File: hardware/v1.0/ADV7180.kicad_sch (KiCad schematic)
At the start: 49 parts, among them J2 Conn_01x03, J3 Conn_01x04, J4 Conn_01x03, J5 Conn_01x34, U2 AMS1117-1.8, U3 ADV7180BCP32Z-RL, U4 TLV62585, Y1 28.63636MHz

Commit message: backup
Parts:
- removed D2: LED, LED_SMD:LED_0805_2012Metric, symbol Device:LED
- removed R7, R8: 270, Resistor_SMD:R_0603_1608Metric, symbol Device:R_Small
- J5: renamed from J2; footprint (none) -> Connector_PinHeader_2.54mm:PinHeader_1x03_P2.54mm_Vertical
- J6: renamed from J4; footprint (none) -> Connector_PinHeader_2.54mm:PinHeader_1x03_P2.54mm_Vertical
- renumbered C20 to C10, C12 to C11, C13 to C12, C16 to C13, C17 to C14, C14 to C15, C18 to C16, C21 to C17, C10 to C18, C11 to C19, C5 to C2, C22 to C20, C15 to C21, C19 to C22, C6 to C3, C2 to C4, C3 to C5, C4 to C6, C8 to C7, C7 to C8, J3 to J7, J5 to J8, R2 to R10, R3 to R11, R4 to R12, R6 to R13, R9 to R14, R10 to R15, R11 to R16, R5 to R8, R1 to R9, U2 to U3, U3 to U4, U4 to U5
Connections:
- net YUV_CLK: now also RN1.5 (R4.2), U4.11 (LLC); no longer J8.2 (Pin_2), RN4.1 (R1.1)
- net YUV_HS: now also RN1.6 (R3.2), U4.1 (HS); no longer J8.3 (Pin_3), RN3.4 (R4.1)
- net YUV_INTRQ: now also RN1.7 (R2.2), U4.32 (~{INTRQ}); no longer J8.4 (Pin_4), RN3.1 (R1.1)
- net YUV_P0: now also RN3.5 (R4.2), U4.16 (P0); no longer J8.22 (Pin_22), RN1.4 (R4.1)
- net YUV_P1: now also RN3.6 (R3.2), U4.15 (P1); no longer J8.23 (Pin_23), RN1.3 (R3.1)
- net YUV_P2: now also RN3.7 (R2.2), U4.10 (P2); no longer J8.24 (Pin_24), RN1.2 (R2.1)
- net YUV_P3: now also RN3.8 (R1.2), U4.9 (P3); no longer J8.25 (Pin_25), RN1.1 (R1.1)
- net YUV_P4: now also RN4.5 (R4.2), U4.8 (P4); no longer J8.26 (Pin_26), RN2.4 (R4.1)
- net YUV_P5: now also RN4.6 (R3.2), U4.7 (P5); no longer J8.27 (Pin_27), RN2.3 (R3.1)
- net YUV_P6: now also RN4.7 (R2.2), U4.6 (P6); no longer J8.28 (Pin_28), RN2.2 (R2.1)
- net YUV_P7: now also RN4.8 (R1.2), U4.5 (P7); no longer J8.29 (Pin_29), RN2.1 (R1.1)
- net YUV_SFL: now also RN2.5 (R4.2), U4.4 (SFL); no longer J8.6 (Pin_6), RN3.2 (R2.1)
- net YUV_VS: now also RN1.8 (R1.2), U4.31 (VS/FIELD); no longer J8.5 (Pin_5), RN3.3 (R3.1)
- net at RN2.6 (R3.2): no longer U4.7 (P5)
- net at RN2.7 (R2.2): no longer U4.6 (P6)
- net at RN2.8 (R1.2): no longer U4.5 (P7)
- net at RN4.2 (R2.1): now also J8.28 (Pin_28)
- net at RN4.3 (R3.1): now also J8.27 (Pin_27)
- net at RN4.4 (R4.1): now also J8.26 (Pin_26)
- new net: J8.29 (Pin_29), RN4.1 (R1.1)
- new net: J8.5 (Pin_5), RN1.1 (R1.1)
- new net: J8.4 (Pin_4), RN1.2 (R2.1)
- new net: J8.3 (Pin_3), RN1.3 (R3.1)
- new net: J8.2 (Pin_2), RN1.4 (R4.1)
- new net: J8.22 (Pin_22), RN3.4 (R4.1)
- new net: J8.23 (Pin_23), RN3.3 (R3.1)
- new net: J8.24 (Pin_24), RN3.2 (R2.1)
- new net: J8.25 (Pin_25), RN3.1 (R1.1)
- new net: J8.6 (Pin_6), RN2.4 (R4.1)
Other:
- moved on the sheet: J7, J8

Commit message: changes
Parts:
- added C40: 0.1uf, Capacitor_SMD:C_0603_1608Metric, symbol Device:C_Small
- added R36, R37: 4.7K, Resistor_SMD:R_0603_1608Metric, symbol Device:R_Small
- added TP1: VCC_PAD, TestPoint:TestPoint_Pad_D1.5mm, symbol Connector:TestPoint_Flag
- added TP2: SWIO_PAD, TestPoint:TestPoint_Pad_D1.5mm, symbol Connector:TestPoint_Flag
- added TP3: GND_PAD, TestPoint:TestPoint_Pad_D1.5mm, symbol Connector:TestPoint_Flag
- added U2: CH32V003JxMx, Package_SO:SOP-8_3.9x4.9mm_P1.27mm, symbol MCU_WCH_CH32V0:CH32V003JxMx
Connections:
- net +3V3: now also C40.1, R36.1, R37.1, TP1.1, U2.4 (VDD)
- net GND: now also C40.2, TP3.1, U2.2 (VSS)
- net RST: now also U2.7 (PC4)
- net SCLK: now also R37.2, U2.6 (PC2)
- net SDATA: now also R36.2, U2.5 (PC1)
- new net SWIO: TP2.1, U2.8 (PD1/PD4/PD5)
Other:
- note added: "FPC"
- note added: "MCU"
- note removed: "CONNECTORS"
- moved on the sheet: J7

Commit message: changes
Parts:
- removed C21: 0.1uf, Capacitor_SMD:C_0603_1608Metric, symbol Device:C_Small
- removed C22: 10nf, Capacitor_SMD:C_0603_1608Metric, symbol Device:C_Small
- R15, R16: footprint Resistor_SMD:R_0402_1005Metric -> Resistor_SMD:R_0603_1608Metric
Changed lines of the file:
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@@
 	(rectangle
 		(start 59.69 144.78)
-		(end 116.84 172.72)
+		(end 111.76 172.72)
 		(stroke
 			(width 0.508)
@@
 	)
 	(junction
-		(at 95.25 162.56)
-		(diameter 0)
-		(color 0 0 0 0)
-	)
-	(junction
 		(at 152.4 114.3)
 		(diameter 0)
@@
 	)
 	(junction
-		(at 104.14 167.64)
-		(diameter 0)
-		(color 0 0 0 0)
-	)
-	(junction
 		(at 107.315 125.095)
 		(diameter 0)
@@
 	)
 	(junction
-		(at 104.14 162.56)
-		(diameter 0)
-		(color 0 0 0 0)
-	)
-	(junction
 		(at 41.91 73.66)
 		(diameter 0)
@@
 	)
 	(junction
-		(at 95.25 167.64)
-		(diameter 0)
-		(color 0 0 0 0)
-	)
-	(junction
 		(at 73.66 78.74)
 		(diameter 0)
@@
 	(wire
 		(pts
-			(xy 95.25 167.64) (xy 104.14 167.64)
-		)
-		(stroke
-			(width 0)
-			(type default)
-		)
-	)
-	(wire
-		(pts
 			(xy 78.74 78.74) (xy 76.2 78.74)
 		)
@@
 		)
 	)
-	(wire
-		(pts
-			(xy 104.14 162.56) (xy 113.03 162.56)
-		)
-		(stroke
-			(width 0)
-			(type default)
-		)
-	)
 	(bus
 		(pts
@@
 	(wire
 		(pts
-			(xy 95.25 162.56) (xy 104.14 162.56)
-		)
-		(stroke
-			(width 0)
-			(type default)
-		)
-	)
-	(wire
-		(pts
 			(xy 52.07 102.87) (xy 52.07 104.14)
 		)
@@
 	(wire
 		(pts
-			(xy 104.14 167.64) (xy 113.03 167.64)
-		)
-		(stroke
-			(width 0)
-			(type default)
-		)
-	)
-	(wire
-		(pts
 			(xy 153.67 88.9) (xy 156.21 88.9)
 		)
@@
 			)
 		)
-		(property "Footprint" "Resistor_SMD:R_0402_1005Metric"
+		(property "Footprint" "Resistor_SMD:R_0603_1608Metric"
 			(at 107.315 127.635 0)
 			(effects
@@
 			)
 		)
-		(property "Footprint" "Resistor_SMD:R_0402_1005Metric"
+		(property "Footprint" "Resistor_SMD:R_0603_1608Metric"
 			(at 107.315 133.985 0)
 			(effects
@@
 	)
 	(symbol
-		(lib_id "Device:C_Small")
-		(at 113.03 165.1 0)
-		(unit 1)
-		(exclude_from_sim no)
-		(in_bom yes)
-		(on_board yes)
-		(dnp no)
-		(property "Reference" "C22"
-			(at 111.125 166.37 0)
-			(effects
-				(font
-					(size 1.27 1.27)
-				)
-				(justify right)
-			)
-		)
-		(property "Value" "10nf"
-			(at 111.125 164.465 0)
-			(effects
-				(font
-					(size 1.27 1.27)
-				)
-				(justify right)
-			)
-		)
-		(property "Footprint" "Capacitor_SMD:C_0603_1608Metric"
-			(at 113.03 165.1 0)
-			(effects
-				(font
-					(size 1.27 1.27)
-				)
-				(hide yes)
-			)
-		)
-		(property "Datasheet" "~"
-			(at 113.03 165.1 0)
-			(effects
-				(font
-					(size 1.27 1.27)
-				)
-				(hide yes)
-			)
-		)
-		(property "Description" ""
-			(at 113.03 165.1 0)
-			(effects
-				(font
-					(size 1.27 1.27)
-				)
-				(hide yes)
-			)
-		)
-		(pin "1"
-		)
-		(pin "2"
-		)
-		(instances
-			(project "QMTECH_XC7A100T-Expantion-Board"
-				(path "/1a66a179-6cc4-4048-836e-3eb434e9da88/856c4711-f246-4385-ad64-862f60e59bf4"
-					(reference "C22")
-					(unit 1)
-				)
-			)
-		)
-	)
-	(symbol
 		(lib_id "power:GND")
 		(at 68.58 154.94 0)
@@
 					(unit 1)
 				)
-			)
-		)
-	)
-	(symbol
-		(lib_id "Device:C_Small")
-		(at 104.14 165.1 0)
-		(unit 1)
-		(exclude_from_sim no)
-		(in_bom yes)
-		(on_board yes)
-		(dnp no)
-		(property "Reference" "C21"
-			(at 102.235 166.37 0)
-			(effects
-				(font
-					(size 1.27 1.27)
-				)
-				(justify right)
-			)
-		)
-		(property "Value" "0.1uf"
-			(at 102.235 164.465 0)
-			(effects
-				(font
-					(size 1.27 1.27)
-				)
-				(justify right)
-			)
-		)
-		(property "Footprint" "Capacitor_SMD:C_0603_1608Metric"
-			(at 104.14 165.1 0)
-			(effects
-				(font
-					(size 1.27 1.27)
-				)
-				(hide yes)
-			)
-		)
-		(property "Datasheet" "~"
-			(at 104.14 165.1 0)
-			(effects
-				(font
-					(size 1.27 1.27)
-				)
-				(hide yes)
-			)
-		)
-		(property "Description" ""
-			(at 104.14 165.1 0)
-			(effects
-				(font
-					(size 1.27 1.27)
-				)
-				(hide yes)
-			)
-		)
-		(pin "1"
-		)
-		(pin "2"
-		)
-		(instances
-			(project "QMTECH_XC7A100T-Expantion-Board"
-				(path "/1a66a179-6cc4-4048-836e-3eb434e9da88/856c4711-f246-4385-ad64-862f60e59bf4"
-					(reference "C21")
-					(unit 1)
-				)

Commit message: backup
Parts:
- removed C1, C9: 10uf, Capacitor_SMD:C_0805_2012Metric, symbol Device:C_Small
- removed C17: 22uf, Capacitor_SMD:C_0805_2012Metric, symbol Device:C_Small
- removed D1: LED, LED_SMD:LED_0805_2012Metric, symbol Device:LED
- removed U3: AMS1117-1.8, Package_TO_SOT_SMD:SOT-223-3_TabPin2, symbol Regulator_Linear:AMS1117-1.8
- added D1: ~, C779813:LED-SMD_4P-L1.6-W1.5-BR_TZ-P4-1615, symbol Device:LED_ARGB
- added U13: TLV75718PDRV, Package_SON:WSON-6-1EP_2x2mm_P0.65mm_EP1x1.6mm, symbol Regulator_Linear:TLV75718PDRV
- C10: value 22uf -> 4.7uf
- C20: value 22uf -> 10uf
- C4, C8: value 0.1uf -> 1uf
- L1: value 1uh -> 2.2uh
- R15: value 450K -> 450k
- R16: value 100K -> 100k
- R36, R37: value 4.7K -> 4.7k
- R8: value 10K -> 10k
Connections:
- net +1V8: now also U13.1 (OUT)
- net +3V3: now also U13.4 (EN), U13.6 (IN)
- net GND: now also D1.2 (RK), U13.3 (GND), U13.7 (GND)
- net at R13.1: now also D1.1 (A)
- net STATUS: now reaches U2.3 (PA2)
- net STATUS: now also D1.3 (GK)
- no-connect marks 23 -> 24
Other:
- moved on the sheet: C10, C20, L1, R13, R15, R16, U5

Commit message: changes
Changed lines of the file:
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@@
 		(stroke
 			(width 0)
-			(type dash)
+			(type solid)
 		)
 		(fill
@@
 		(stroke
 			(width 0)
-			(type dash)
+			(type solid)
 		)
 		(fill
@@
 		(stroke
 			(width 0)
-			(type dash)
+			(type solid)
 		)
 		(fill

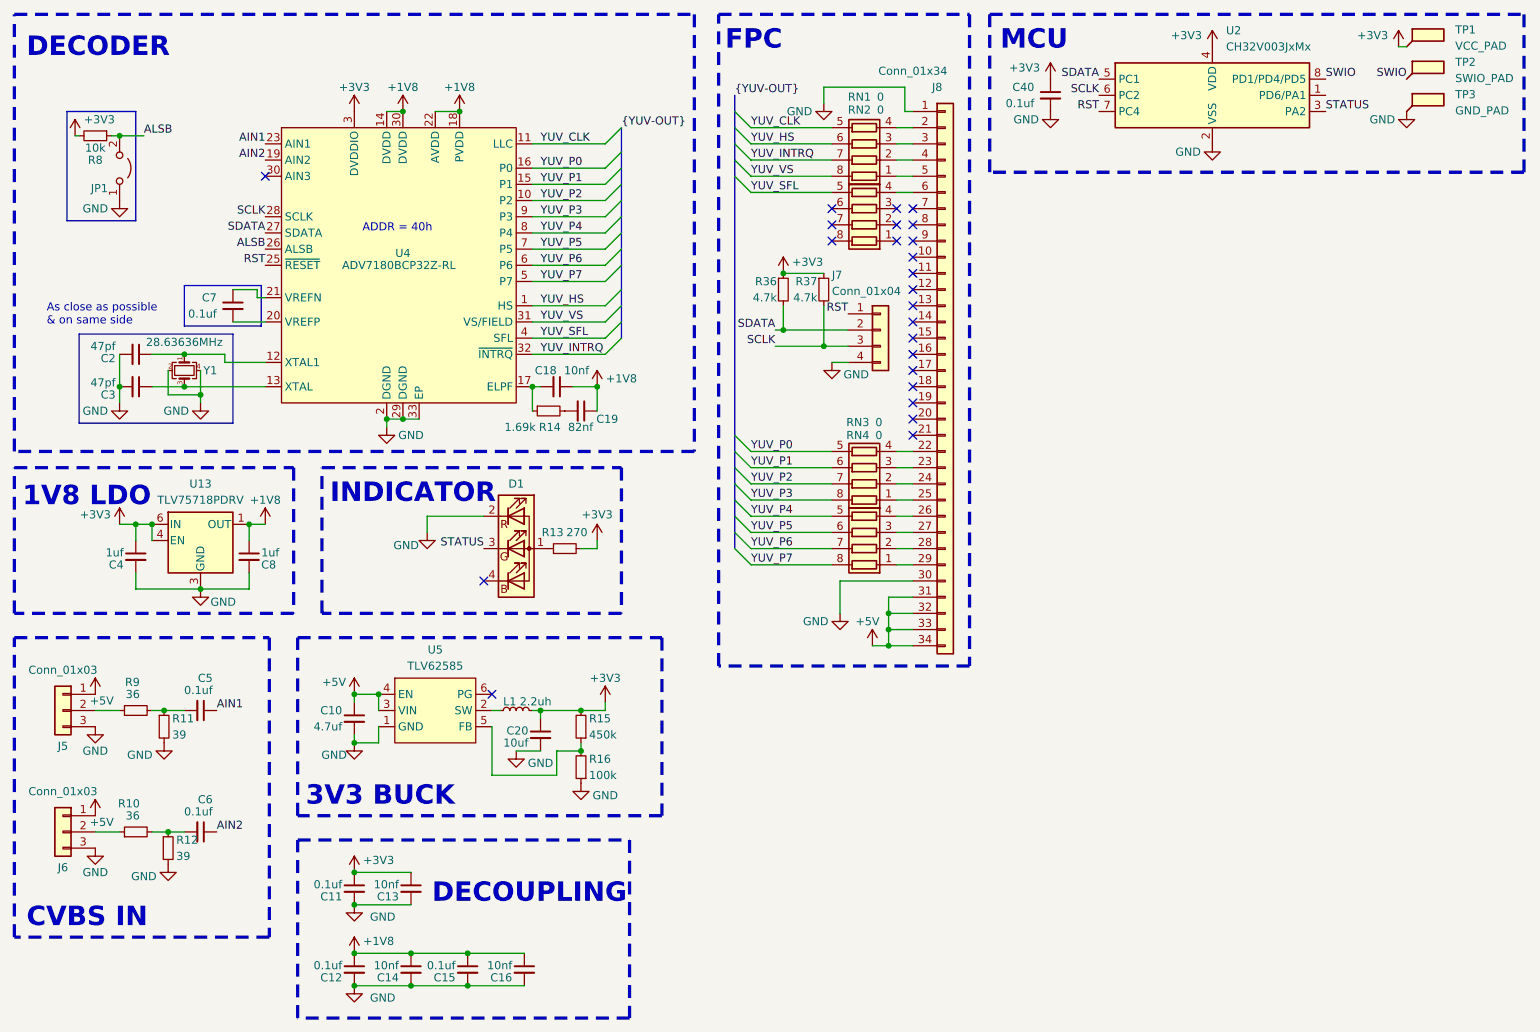
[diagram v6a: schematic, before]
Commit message: added pmod connectors instead of leds
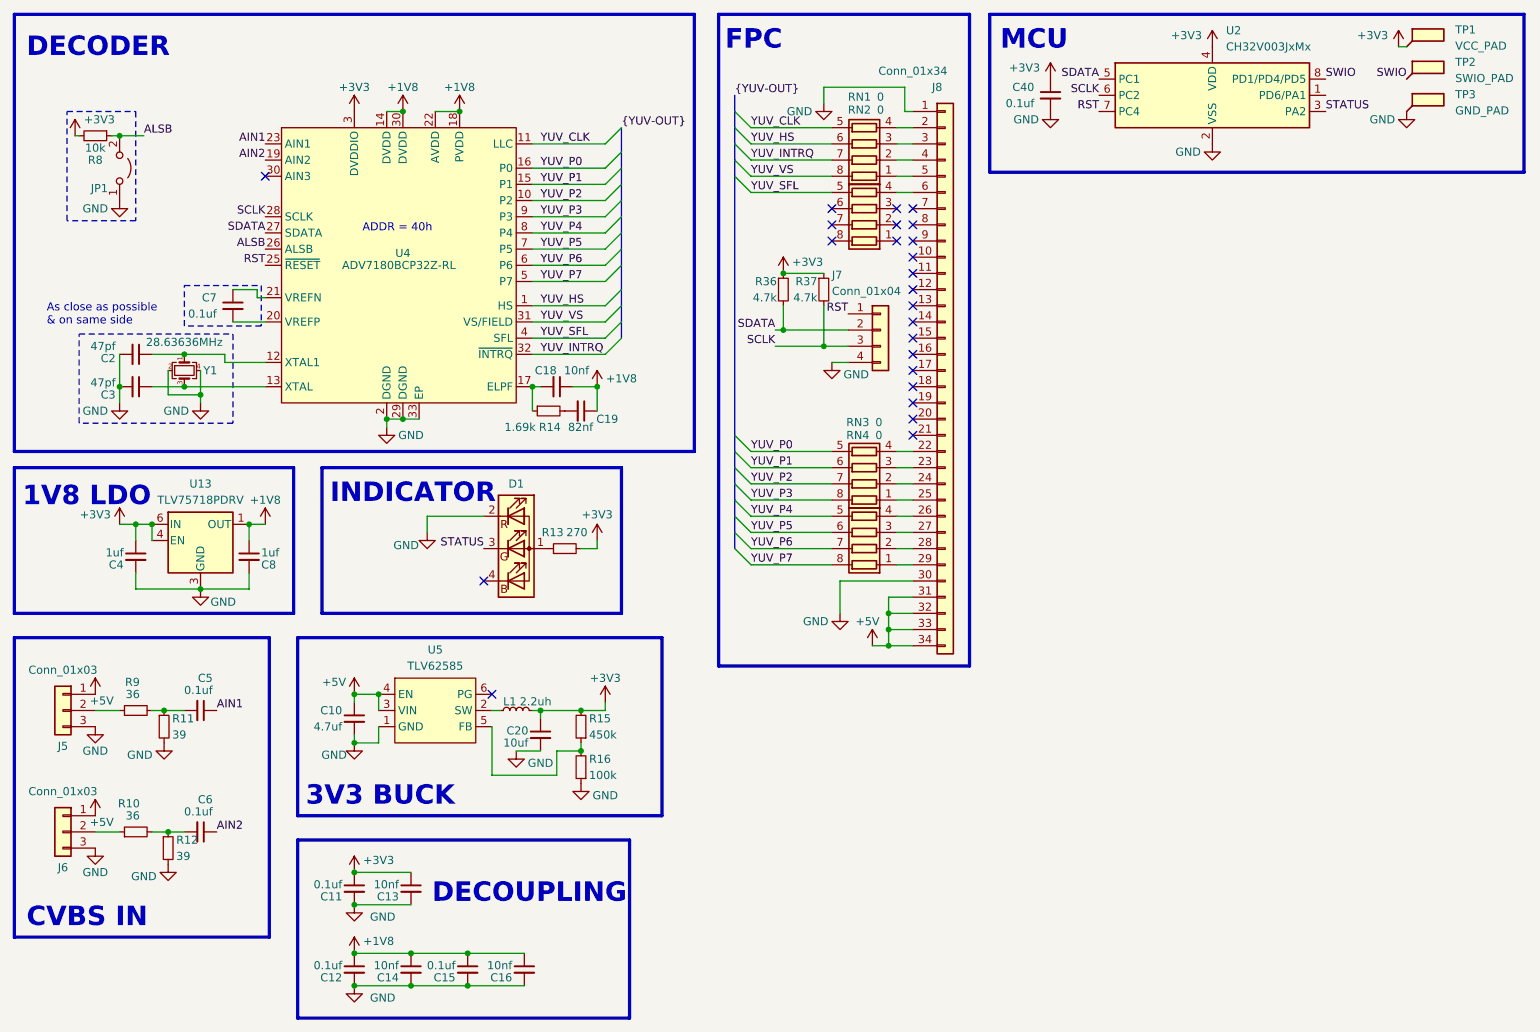
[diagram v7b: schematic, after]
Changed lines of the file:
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@@
 		(stroke
 			(width 0.508)
-			(type dash)
+			(type solid)
 		)
 		(fill
@@
 		(stroke
 			(width 0.508)
-			(type dash)
+			(type solid)
 		)
 		(fill
@@
 		(stroke
 			(width 0.508)
-			(type dash)
+			(type solid)
 		)
 		(fill
@@
 		(stroke
 			(width 0.508)
-			(type dash)
+			(type solid)
 		)
 		(fill
@@
 		(stroke
 			(width 0.508)
-			(type dash)
+			(type solid)
 		)
 		(fill
@@
 		(stroke
 			(width 0)
-			(type solid)
+			(type dash)
 		)
 		(fill
@@
 		(stroke
 			(width 0)
-			(type solid)
+			(type dash)
 		)
 		(fill
@@
 		(stroke
 			(width 0)
-			(type solid)
+			(type dash)
 		)
 		(fill
@@
 		(stroke
 			(width 0.508)
-			(type dash)
+			(type solid)
 		)
 		(fill
@@
 		(stroke
 			(width 0.508)
-			(type dash)
+			(type solid)
 		)
 		(fill
@@
 		(stroke
 			(width 0.508)
-			(type dash)
+			(type solid)
 		)
 		(fill

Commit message: first schematic iteration done
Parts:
- removed R36, R37: 4.7k, Resistor_SMD:R_0603_1608Metric, symbol Device:R_Small
- added RN22: 5.1k, symbol Device:R_Pack02
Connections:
- net +3V3: now also RN22.1 (R1.1), RN22.2 (R2.1)
- net SCLK: now also RN22.4 (R1.2)
- net SDATA: now also RN22.3 (R2.2)
